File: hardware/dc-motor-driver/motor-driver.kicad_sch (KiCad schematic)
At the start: 12 parts, among them J15 MOT, J3 IMODE, U1 DRV8874PWPR

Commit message: initial pcb routing
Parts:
- C3: renamed from 100mF1; value C6 -> 100uF; footprint Capacitor_SMD:C_0402_1005Metric_Pad0.74x0.62mm_HandSolder -> Capacitor_SMD:CP_Elec_6.3x7.7; Supplier (none) -> Digikey; Supplier_link (none) -> https://www.digikey.com.au/en/products/detail/w%C3%BCrth-el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; Supplier_part_number (none) -> 732-8511-1-ND
- J2: renamed from J3; footprint TerminalBlock_4Ucon:TerminalBlock_4Ucon_1x02_P3.50mm_Horizontal -> Connector_PinHeader_2.54mm:PinHeader_1x03_P2.54mm_Vertical
- renumbered C3 to C4, C18 to C5, C5 to C6, J15 to J3
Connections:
- net at U1.10 (OUT2): now also J3.1 (Pin_1); no longer J3.2 (Pin_2)
- net at U1.8 (OUT1): now also J3.2 (Pin_2); no longer J3.1 (Pin_1)
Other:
- moved on the sheet: J3

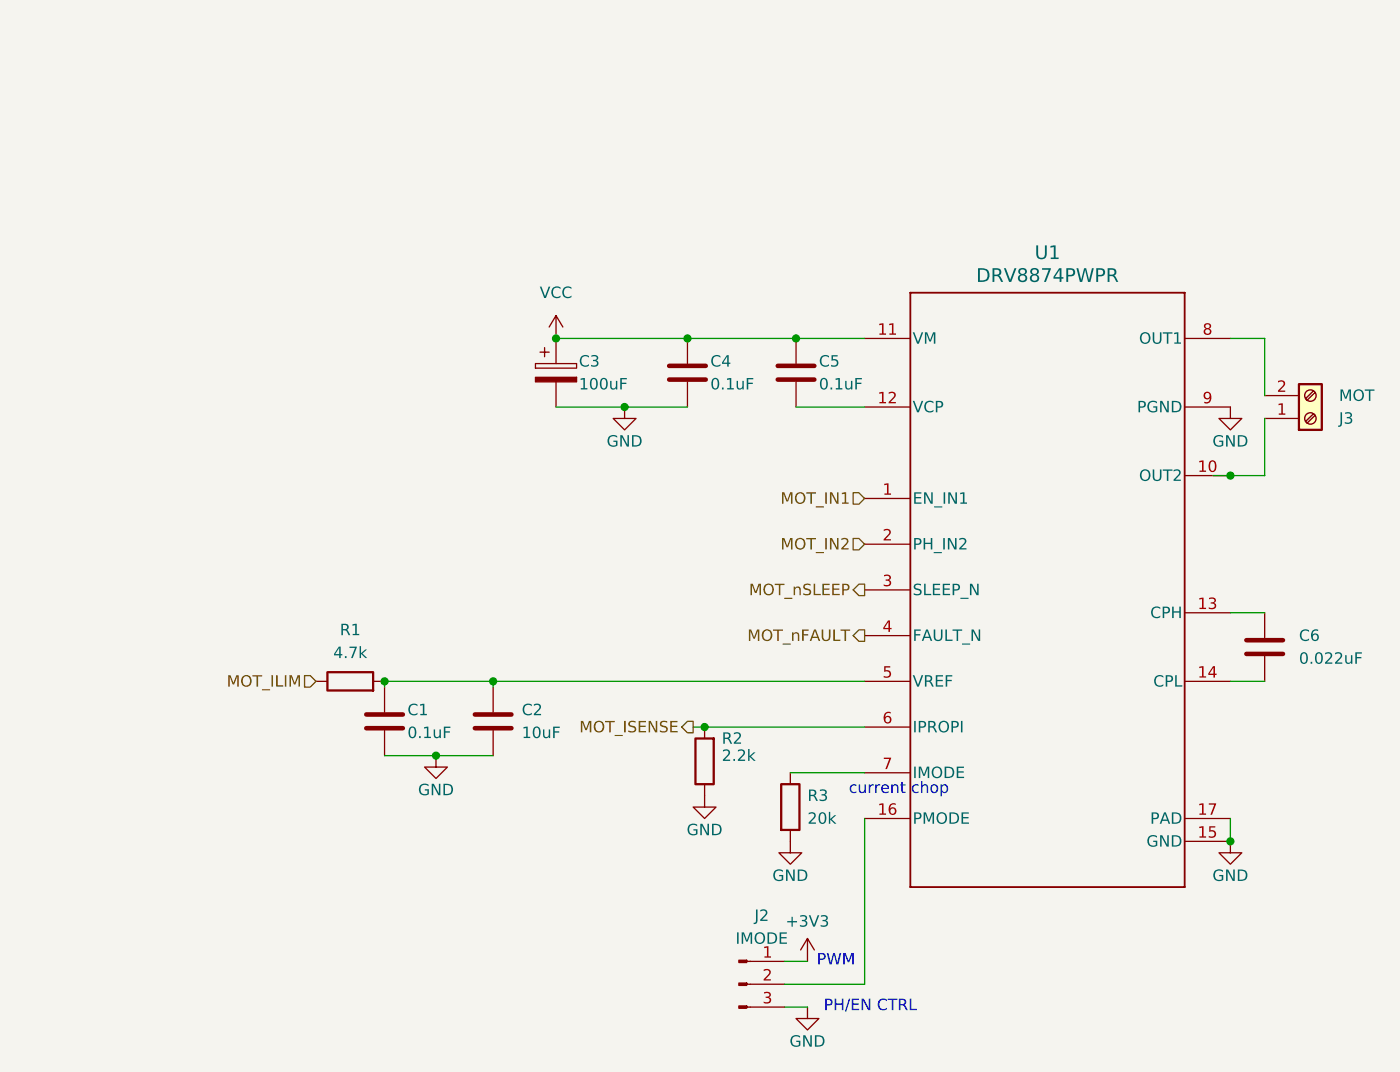
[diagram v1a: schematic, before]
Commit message: feat: WIP PCB layout
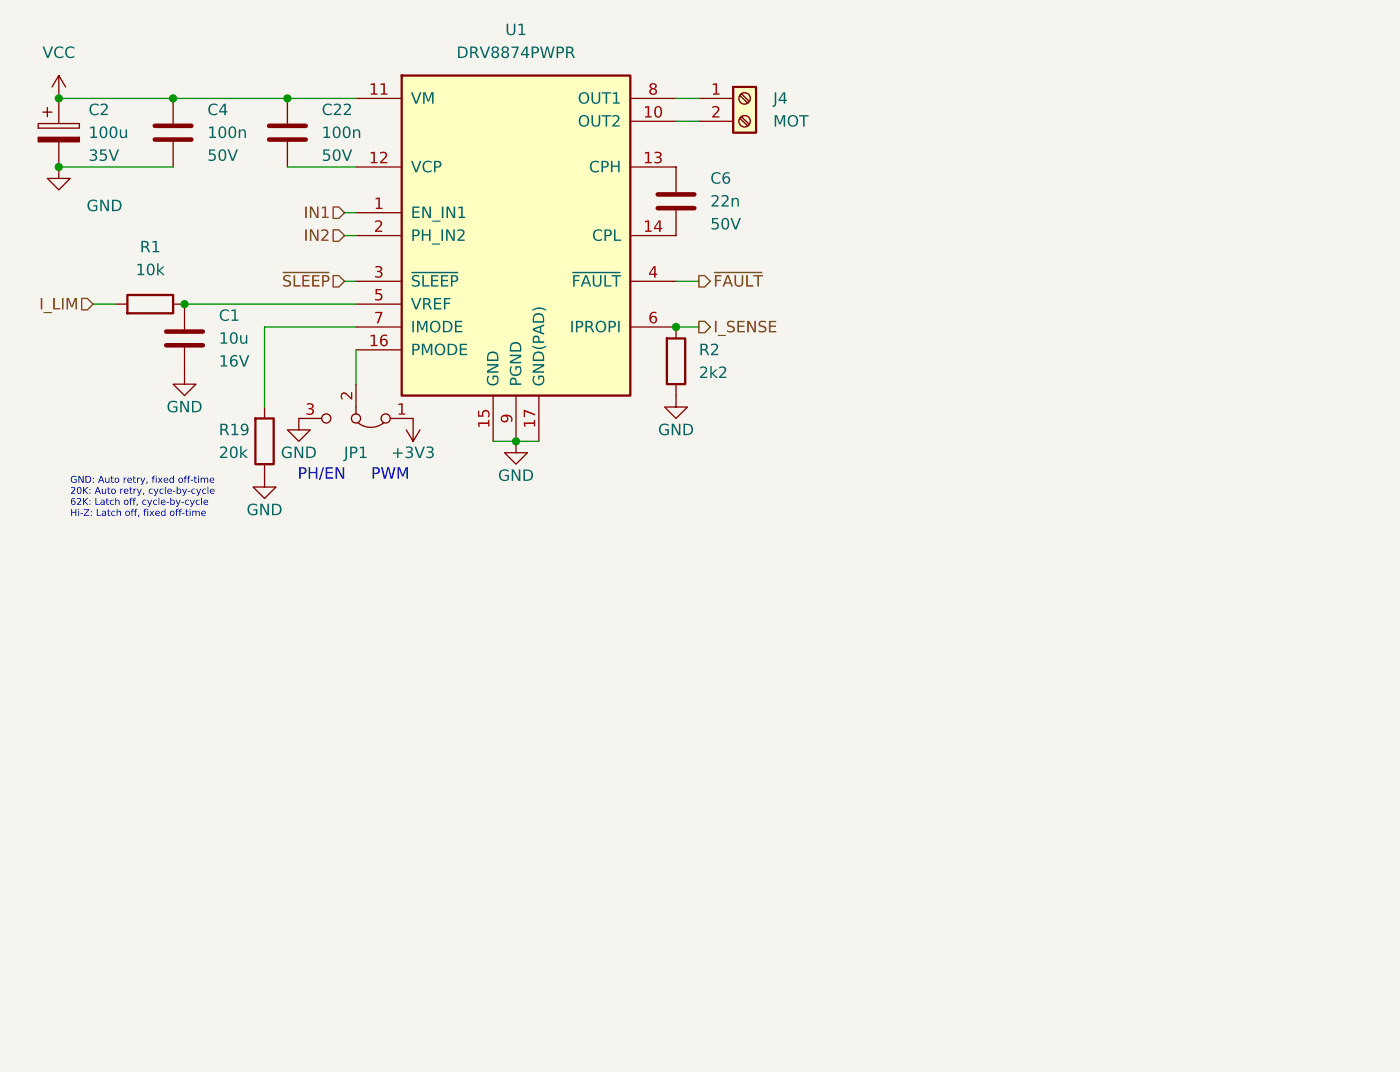
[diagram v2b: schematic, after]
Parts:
- removed C1, C4, C5: 0.1uF, Capacitor_SMD:C_0402_1005Metric_Pad0.74x0.62mm_HandSolder, symbol Device:C
- removed C2: 10uF, Capacitor_SMD:C_0402_1005Metric_Pad0.74x0.62mm_HandSolder, symbol Device:C
- removed C3: 100uF, Capacitor_SMD:CP_Elec_6.3x7.7, symbol Device:C_Polarized
- removed C6: 0.022uF, Capacitor_SMD:C_0402_1005Metric_Pad0.74x0.62mm_HandSolder, symbol Device:C
- removed J2: IMODE, Connector_PinHeader_2.54mm:PinHeader_1x03_P2.54mm_Vertical, symbol Connector:Conn_01x03_Pin
- removed R1: 4.7k, Resistor_SMD:R_0201_0603Metric_Pad0.64x0.40mm_HandSolder, symbol Device:R
- removed R2: 2.2k, Resistor_SMD:R_0201_0603Metric_Pad0.64x0.40mm_HandSolder, symbol Device:R
- removed R3: 20k, Resistor_SMD:R_0201_0603Metric_Pad0.64x0.40mm_HandSolder, symbol Device:R
- removed U1: DRV8874PWPR, Package_DFN_QFN:DRV8874PWPR, symbol 2025-04-07_10-39-51:DRV8874PWPR
- added C1: 10u, Capacitor_SMD:C_0805_2012Metric, symbol Capacitor:C_10u_16V_0805
- added C2: 100u, Capacitor_SMD:CP_Elec_6.3x7.7, symbol Capacitor:C_100u_35V
- added C22, C4: 100n, Capacitor_SMD:C_0603_1608Metric, symbol Capacitor:C_100n_50V_0603
- added C6: 22n, Capacitor_SMD:C_0603_1608Metric, symbol Capacitor:C_22n_50V_0603
- added JP1: Jumper_3_Bridged12, Jumper:SolderJumper-3_P1.3mm_Bridged12_RoundedPad1.0x1.5mm, symbol Jumper:Jumper_3_Bridged12
- added R1: 10k, Resistor_SMD:R_0603_1608Metric, symbol Resistor:R_10k_0603
- added R19: 20k, Resistor_SMD:R_0603_1608Metric, symbol Resistor:R_20k_0603
- added R2: 2k2, Resistor_SMD:R_0603_1608Metric, symbol Resistor:R_2k2_0603
- added U1: DRV8874PWPR, Package_SO:HTSSOP-16-1EP_4.4x5mm_P0.65mm_EP3.4x5mm_Mask2.66x2.46mm_ThermalVias, symbol PMIC_MotorDriver:DRV8874PWPR
- renumbered J3 to J4
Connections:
- net +3V3: now also JP1.1 (A)
- net GND: now also C1.2, C2.2, C4.2, JP1.3 (B), R19.2, R2.2, U1.15 (GND), U1.17 (GND(PAD)), U1.9 (PGND)
- net VCC: now also C2.1, C22.1, C4.1, U1.11 (VM)
- net at J4.1 (Pin_1): now also U1.8 (OUT1)
- net at J4.2 (Pin_2): now also U1.10 (OUT2)
- new net: C22.2, U1.12 (VCP)
- new net: C6.1, U1.13 (CPH)
- new net: C6.2, U1.14 (CPL)
- new net: JP1.2 (C), U1.16 (PMODE)
- new net: C1.1, R1.2, U1.5 (VREF)
- new net: R19.1, U1.7 (IMODE)
- new net IN1: U1.1 (EN_IN1)
- new net IN2: U1.2 (PH_IN2)
- new net I_LIM: R1.1
- new net I_SENSE: R2.1, U1.6 (IPROPI)
- new net ~{FAULT}: U1.4 (~{FAULT})
- new net ~{SLEEP}: U1.3 (~{SLEEP})
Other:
- note added: "GND: Auto retry, fixed off-time 20K: Auto retry, cycle-by-cycle 62K: Latch off, cycle-by-cycle Hi-Z: Latch off, fixed off-time"
- note added: "PH/EN"
- note removed: "PH/EN CTRL"
- note removed: "current chop"
- moved on the sheet: J4

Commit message: feat: Layout done
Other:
- title: (none) -> Motor Driver
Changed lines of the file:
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@@
 	(generator_version "9.0")
 	(paper "A4")
+	(title_block
+		(title "Motor Driver")
+		(rev "V0R1")
+	)
 	(text "PWM"
 		(exclude_from_sim no)

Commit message: Added new mosfet and silkscreen, DRC and ERC passing
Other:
- company: (none) -> QUTRC
- title: Motor Driver -> DC Motor Driver
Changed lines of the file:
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@@
 	(paper "A4")
 	(title_block
-		(title "Motor Driver")
+		(title "DC Motor Driver")
+		(date "2025-12-02")
 		(rev "V0R1")
+		(company "QUTRC")
 	)
 	(text "PWM"
